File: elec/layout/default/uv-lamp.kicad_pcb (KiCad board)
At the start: 2 copper layers, 21 x 21 mm, 3 parts, among them U1 ?, U2 ?, U3 ?

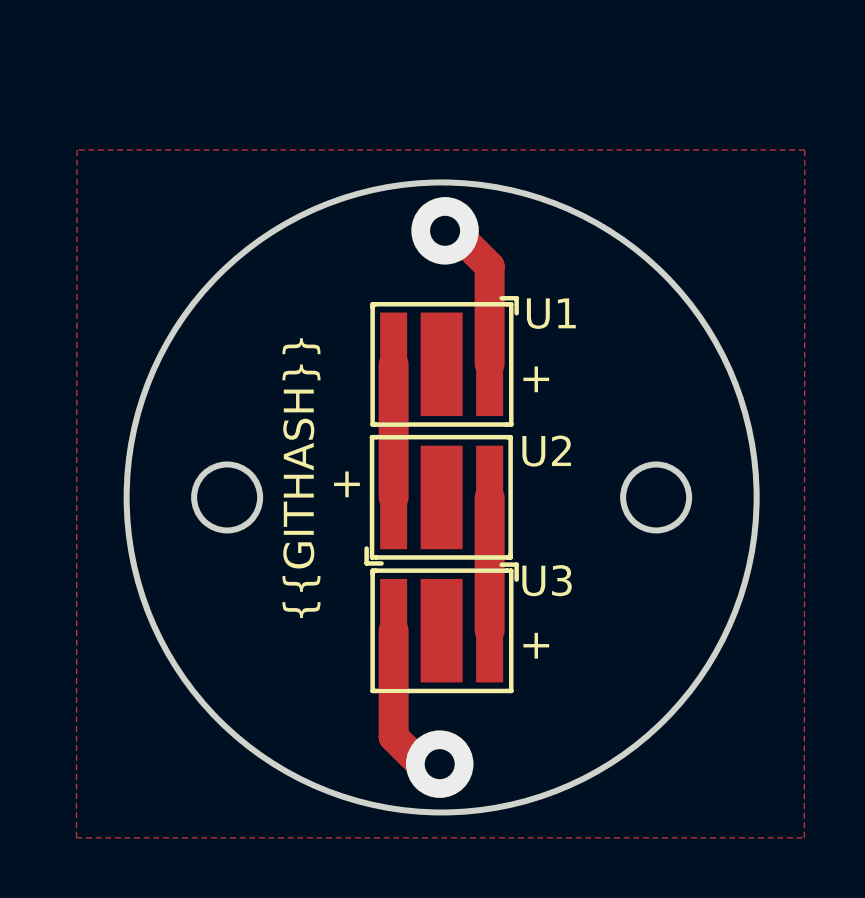
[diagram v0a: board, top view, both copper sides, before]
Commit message: adding notches to driver
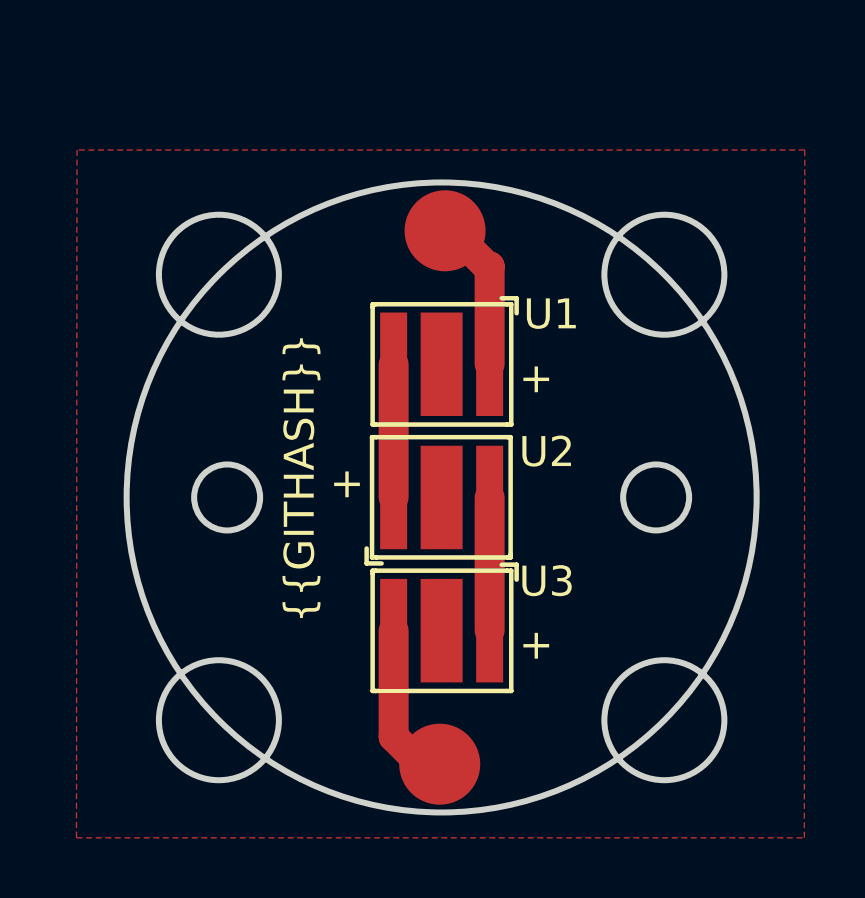
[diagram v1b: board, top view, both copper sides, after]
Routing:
- net gnd: track 5.58 -> 5.45 mm, vias 1 -> 0
- net vcc: track 5.36 -> 5.40 mm, vias 1 -> 0
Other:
- outline, holes or cut-outs redrawn
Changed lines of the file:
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@@
+	)
+	(gr_circle
+		(center 148.004527 77.420557)
+		(end 149.254527 77.420557)
+		(stroke
+			(width 0.2)
+			(type solid)
+		)
+		(fill solid)
+		(layer "F.Cu")
+		(net 4)
+	)
+	(gr_circle
+		(center 147.826005 95.201)
+		(end 149.076005 95.201)
+		(stroke
+			(width 0.2)
+			(type solid)
+		)
+		(fill solid)
+		(layer "F.Cu")
+		(net 7)
+	)
+	(gr_circle
+		(center 155.314621 78.885379)
+		(end 157.314621 78.885379)
+		(stroke
+			(width 0.2)
+			(type default)
+		)
+		(fill none)
+		(layer "Edge.Cuts")
 	)
 	(gr_circle
@@
 	)
 	(gr_circle
+		(center 140.465379 93.734621)
+		(end 142.465379 93.734621)
+		(stroke
+			(width 0.2)
+			(type default)
+		)
+		(fill none)
+		(layer "Edge.Cuts")
+	)
+	(gr_circle
 		(center 140.74 86.31)
 		(end 141.84 86.31)
+		(stroke
+			(width 0.2)
+			(type default)
+		)
+		(fill none)
+		(layer "Edge.Cuts")
+	)
+	(gr_circle
+		(center 155.314621 93.734621)
+		(end 157.314621 93.734621)
+		(stroke
+			(width 0.2)
+			(type default)
+		)
+		(fill none)
+		(layer "Edge.Cuts")
+	)
+	(gr_circle
+		(center 140.465379 78.885379)
+		(end 142.465379 78.885379)
 		(stroke
 			(width 0.2)
@@
 	)
 	(segment
-		(start 149.49 78.60703)
-		(end 148.004527 77.121557)
+		(start 148.075 77.275)
+		(end 149.40703 78.60703)
+		(width 1)
+		(layer "F.Cu")
+		(net 4)
+	)
+	(segment
+		(start 148.004527 77.420557)
+		(end 148.004527 77.345473)
 		(width 1)
 		(layer "F.Cu")
@@
 		(net 4)
 	)
-	(via
-		(at 148.004527 77.421557)
-		(size 2.25)
-		(drill 1)
-		(layers "F.Cu" "B.Cu")
-		(free yes)
-		(teardrops
-			(best_length_ratio 0.5)
-			(max_length 1)
-			(best_width_ratio 1)
-			(max_width 2)
-			(curve_points 0)
-			(filter_ratio 0.9)
-			(enabled yes)
-			(allow_two_segments yes)
-			(prefer_zone_connections yes)
-		)
+	(segment
+		(start 149.40703 78.60703)
+		(end 149.49 78.60703)
+		(width 1)
+		(layer "F.Cu")
+		(net 4)
+	)
+	(segment
+		(start 148.004527 77.345473)
+		(end 148.075 77.275)
+		(width 1)
+		(layer "F.Cu")
 		(net 4)
 	)
@@
 	)
 	(segment
+		(start 147.826005 95.201)
+		(end 147.201 95.201)
+		(width 1)
+		(layer "F.Cu")
+		(net 7)
+	)
+	(segment
 		(start 146.29 94.29)
 		(end 146.29 90.75)
@@
 	)
 	(segment
-		(start 147.826005 95.5)
-		(end 147.5 95.5)
-		(width 1)
-		(layer "F.Cu")
-		(net 7)
-	)
-	(segment
-		(start 147.5 95.5)
+		(start 147.201 95.201)
 		(end 146.29 94.29)
 		(width 1)
 		(layer "F.Cu")
-		(net 7)
-	)
-	(via
-		(at 147.826005 95.2)
-		(size 2.25)
-		(drill 1)
-		(layers "F.Cu" "B.Cu")
-		(free yes)
-		(teardrops
-			(best_length_ratio 0.5)
-			(max_length 1)
-			(best_width_ratio 1)
-			(max_width 2)
-			(curve_points 0)
-			(filter_ratio 0.9)
-			(enabled yes)
-			(allow_two_segments yes)
-			(prefer_zone_connections yes)
-		)
 		(net 7)
 	)
@@
 			)
 		)
-	)
-	(zone
-		(net 0)
-		(net_name "")
-		(layer "F.Cu")
-		(name "$teardrop_padvia$")
-		(hatch full 0.1)
-		(priority 30000)
-		(attr
-			(teardrop
-				(type padvia)
-			)
-		)
-		(connect_pads yes
-			(clearance 0)
-		)
-		(min_thickness 0.0254)
-		(filled_areas_thickness no)
-		(fill yes
-			(thermal_gap 0.5)
-			(thermal_bridge_width 0.5)
-			(island_removal_mode 1)
-			(island_area_min 10)
-		)
-		(polygon
-			(pts
-				(xy 148.99 78.808537) (xy 149.99 78.808537) (xy 149.062304 77.040318) (xy 148.004527 77.420557)
-				(xy 147.809173 78.529466)
-			)
-		)
-	)
-	(zone
-		(net 0)
-		(net_name "")
-		(layer "F.Cu")
-		(name "$teardrop_padvia$")
-		(hatch full 0.1)
-		(priority 30001)
-		(attr
-			(teardrop
-				(type padvia)
-			)
-		)
-		(connect_pads yes
-			(clearance 0)
-		)
-		(min_thickness 0.0254)
-		(filled_areas_thickness no)
-		(fill yes
-			(thermal_gap 0.5)
-			(thermal_bridge_width 0.5)
-			(island_removal_mode 1)
-			(island_area_min 10)
-		)
-		(polygon
-			(pts
-				(xy 146.79 93.991203) (xy 145.79 93.991203) (xy 146.828693 95.688423) (xy 147.826005 95.201) (xy 148.021359 94.092091)
-			)
-		)
-	)
-	(zone
-		(net 4)
-		(net_name "vcc")
-		(layer "F.Cu")
-		(name "$teardrop_padvia$")
-		(hatch full 0.1)
-		(priority 30000)
-		(attr
-			(teardrop
-				(type padvia)
-			)
-		)
-		(connect_pads yes
-			(clearance 0)
-		)
-		(min_thickness 0.0254)
-		(filled_areas_thickness no)
-		(fill yes
-			(thermal_gap 0.5)
-			(thermal_bridge_width 0.5)
-			(island_removal_mode 1)
-			(island_area_min 10)
-		)
-		(polygon
-			(pts
-				(xy 148.99 78.808537) (xy 149.99 78.808537) (xy 149.062304 77.040318) (xy 148.004527 77.420557)
-				(xy 147.809173 78.529466)
-			)
-		)
-	)
-	(zone
-		(net 4)
-		(net_name "vcc")
-		(layer "F.Cu")
-		(name "$teardrop_padvia$")
-		(hatch full 0.1)
-		(priority 30000)
-		(attr
-			(teardrop
-				(type padvia)
-			)
-		)
-		(connect_pads yes
-			(clearance 0)
-		)
-		(min_thickness 0.0254)
-		(filled_areas_thickness no)
-		(fill yes
-			(thermal_gap 0.5)
-			(thermal_bridge_width 0.5)
-			(island_removal_mode 1)
-			(island_area_min 10)
-		)
-		(polygon
-			(pts
-				(xy 148.99 78.808537) (xy 149.99 78.808537) (xy 149.062304 77.040318) (xy 148.004527 77.420557)
-				(xy 147.809173 78.529466)
-			)
-		)

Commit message: new uv PCB
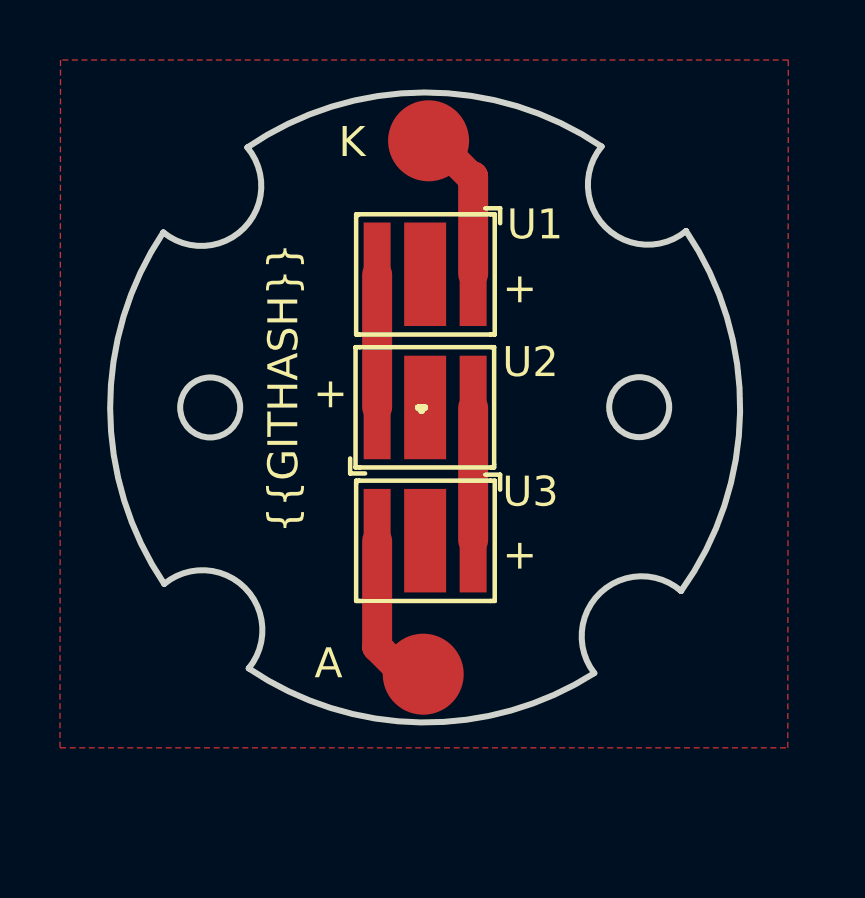
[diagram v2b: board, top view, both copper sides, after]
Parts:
- moved U1 3.05 mm to (147.3, 78.9)
- moved U2 3.05 mm to (147.3, 83.3)
- moved U3 3.05 mm to (147.3, 87.8)
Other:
- outline, holes or cut-outs redrawn
- board text added: "A"
- board text added: "K"
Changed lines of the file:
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@@
 	(footprint "lib:LED-SMD_3P-L3.5-W3.5_M3535O1IRS13G06"
 		(layer "F.Cu")
-		(at 147.89 90.75)
+		(at 147.34 87.75)
 		(property "Reference" "U3"
 			(at 3.51 -1.63 0)
@@
 	(footprint "lib:LED-SMD_3P-L3.5-W3.5_M3535O1IRS13G06"
 		(layer "F.Cu")
-		(at 147.89 81.87)
+		(at 147.34 78.87)
 		(property "Reference" "U1"
 			(at 3.66 -1.66 0)
@@
 	(footprint "lib:LED-SMD_3P-L3.5-W3.5_M3535O1IRS13G06"
 		(layer "F.Cu")
-		(at 147.89 86.31 180)
+		(at 147.34 83.31 180)
 		(property "Reference" "U2"
 			(at -3.51 1.51 0)
@@
 	)
 	(gr_circle
-		(center 148.004527 77.420557)
-		(end 149.254527 77.420557)
+		(center 147.454527 74.420557)
+		(end 148.704527 74.420557)
 		(stroke
 			(width 0.2)
@@
 	)
 	(gr_circle
-		(center 147.826005 95.201)
-		(end 149.076005 95.201)
+		(center 147.276005 92.201)
+		(end 148.526005 92.201)
 		(stroke
 			(width 0.2)
@@
 		(net 7)
 	)
+	(gr_line
+		(start 147.339996 83.310002)
+		(end 147.218594 83.431404)
+		(stroke
+			(width 0.2)
+			(type default)
+		)
+		(layer "F.SilkS")
+	)
+	(gr_line
+		(start 147.339996 83.310002)
+		(end 147.099872 83.310002)
+		(stroke
+			(width 0.2)
+			(type default)
+		)
+		(layer "F.SilkS")
+	)
+	(gr_line
+		(start 147.339996 83.310002)
+		(end 147.099872 83.310002)
+		(stroke
+			(width 0.2)
+			(type default)
+		)
+		(layer "F.SilkS")
+	)
+	(gr_line
+		(start 147.218594 83.431404)
+		(end 147.099872 83.310002)
+		(stroke
+			(width 0.2)
+			(type default)
+		)
+		(layer "F.SilkS")
+	)
 	(gr_circle
-		(center 155.314621 78.885379)
-		(end 157.314621 78.885379)
+		(center 147.454527 74.420557)
+		(end 148.704527 74.420557)
+		(stroke
+			(width 0.2)
+			(type solid)
+		)
+		(fill solid)
+		(layer "F.Mask")
+	)
+	(gr_circle
+		(center 147.276005 92.201)
+		(end 148.526005 92.201)
+		(stroke
+			(width 0.2)
+			(type solid)
+		)
+		(fill solid)
+		(layer "F.Mask")
+	)
+	(gr_arc
+		(start 141.413031 74.64276)
+		(mid 147.312897 72.810037)
+		(end 153.222145 74.612282)
+		(stroke
+			(width 0.2)
+			(type default)
+		)
+		(layer "Edge.Cuts")
+	)
+	(gr_arc
+		(start 152.980661 92.166237)
+		(mid 153.182794 89.483469)
+		(end 155.872617 89.429183)
+		(stroke
+			(width 0.2)
+			(type default)
+		)
+		(layer "Edge.Cuts")
+	)
+	(gr_arc
+		(start 156.037716 77.427853)
+		(mid 157.839003 83.454433)
+		(end 155.872617 89.429183)
+		(stroke
+			(width 0.2)
+			(type default)
+		)
+		(layer "Edge.Cuts")
+	)
+	(gr_circle
+		(center 140.175 83.310002)
+		(end 141.175 83.310002)
 		(stroke
 			(width 0.2)
@@
 		(layer "Edge.Cuts")
 	)
+	(gr_arc
+		(start 152.980661 92.166237)
+		(mid 147.195564 93.809009)
+		(end 141.457847 92.007721)
+		(stroke
+			(width 0.2)
+			(type default)
+		)
+		(layer "Edge.Cuts")
+	)
+	(gr_arc
+		(start 141.413031 74.64276)
+		(mid 141.30115 77.333592)
+		(end 138.611627 77.47343)
+		(stroke
+			(width 0.2)
+			(type default)
+		)
+		(layer "Edge.Cuts")
+	)
+	(gr_arc
+		(start 138.642277 89.192151)
+		(mid 136.840032 83.337464)
+		(end 138.611627 77.47343)
+		(stroke
+			(width 0.2)
+			(type default)
+		)
+		(layer "Edge.Cuts")
+	)
+	(gr_arc
+		(start 156.037716 77.427853)
+		(mid 153.350405 77.299593)
+		(end 153.222145 74.612282)
+		(stroke
+			(width 0.2)
+			(type default)
+		)
+		(layer "Edge.Cuts")
+	)
 	(gr_circle
-		(center 155.04 86.31)
-		(end 156.14 86.31)
+		(center 154.475 83.3)
+		(end 155.475 83.3)
 		(stroke
 			(width 0.2)
@@
 		(layer "Edge.Cuts")
 	)
-	(gr_circle
-		(center 147.89 86.31)
-		(end 158.39 86.31)
-		(stroke
-			(width 0.2)
-			(type default)
-		)
-		(fill none)
+	(gr_arc
+		(start 138.642277 89.192151)
+		(mid 141.329577 89.32042)
+		(end 141.457847 92.007721)
+		(stroke
+			(width 0.2)
+			(type default)
+		)
 		(layer "Edge.Cuts")
 	)
-	(gr_circle
-		(center 140.465379 93.734621)
-		(end 142.465379 93.734621)
-		(stroke
-			(width 0.2)
-			(type default)
-		)
-		(fill none)
-		(layer "Edge.Cuts")
-	)
-	(gr_circle
-		(center 140.74 86.31)
-		(end 141.84 86.31)
-		(stroke
-			(width 0.2)
-			(type default)
-		)
-		(fill none)
-		(layer "Edge.Cuts")
-	)
-	(gr_circle
-		(center 155.314621 93.734621)
-		(end 157.314621 93.734621)
-		(stroke
-			(width 0.2)
-			(type default)
-		)
-		(fill none)
-		(layer "Edge.Cuts")
-	)
-	(gr_circle
-		(center 140.465379 78.885379)
-		(end 142.465379 78.885379)
-		(stroke
-			(width 0.2)
-			(type default)
-		)
-		(fill none)
-		(layer "Edge.Cuts")
+	(gr_text "K"
+		(at 144.454527 75.05 0)
+		(layer "F.SilkS")
+		(effects
+			(font
+				(size 1 1)
+				(thickness 0.15)
+			)
+			(justify left bottom)
+		)
+	)
+	(gr_text "A"
+		(at 143.65 92.425 0)
+		(layer "F.SilkS")
+		(effects
+			(font
+				(size 1 1)
+				(thickness 0.15)
+			)
+			(justify left bottom)
+		)
 	)
 	(gr_text "{{GITHASH}}"
-		(at 143.75 90.5 90)
+		(at 143.2 87.5 90)
 		(layer "F.SilkS")
 		(effects
@@
 	)
 	(segment
-		(start 148.075 77.275)
-		(end 149.40703 78.60703)
+		(start 147.525 74.275)
+		(end 148.85703 75.60703)
 		(width 1)
 		(layer "F.Cu")
@@
 	)
 	(segment
-		(start 148.004527 77.420557)
-		(end 148.004527 77.345473)
+		(start 147.454527 74.420557)
+		(end 147.454527 74.345473)
 		(width 1)
 		(layer "F.Cu")
@@
 	)
 	(segment
-		(start 149.49 81.87)
-		(end 149.49 78.60703)
+		(start 148.94 78.87)
+		(end 148.94 75.60703)
 		(width 1)
 		(layer "F.Cu")
@@
 	)
 	(segment
-		(start 149.40703 78.60703)
-		(end 149.49 78.60703)
+		(start 148.85703 75.60703)
+		(end 148.94 75.60703)
 		(width 1)
 		(layer "F.Cu")
@@
 	)
 	(segment
-		(start 148.004527 77.345473)
-		(end 148.075 77.275)
+		(start 147.454527 74.345473)
+		(end 147.525 74.275)
 		(width 1)
 		(layer "F.Cu")
@@
 	)
 	(segment
-		(start 146.29 81.87)
-		(end 146.29 86.31)
+		(start 145.74 78.87)
+		(end 145.74 83.31)
 		(width 1)
 		(layer "F.Cu")
@@
 	)
 	(segment
-		(start 149.49 90.75)
-		(end 149.49 86.31)
+		(start 148.94 87.75)
+		(end 148.94 83.31)
 		(width 1)
 		(layer "F.Cu")
@@
 	)
 	(segment
-		(start 147.826005 95.201)
-		(end 147.201 95.201)
+		(start 147.276005 92.201)
+		(end 146.651 92.201)
 		(width 1)
 		(layer "F.Cu")
@@
 	)
 	(segment
-		(start 146.29 94.29)
-		(end 146.29 90.75)
+		(start 145.74 91.29)
+		(end 145.74 87.75)
 		(width 1)
 		(layer "F.Cu")
@@
 	)
 	(segment
-		(start 147.201 95.201)
-		(end 146.29 94.29)
+		(start 146.651 92.201)
+		(end 145.74 91.29)
 		(width 1)
 		(layer "F.Cu")
@@
 		(polygon
 			(pts
-				(xy 159.995473 74.727755) (xy 135.735473 74.727755) (xy 135.718641 97.655363) (xy 159.978641 97.655363)
-			)
-		)
-	)
+				(xy 159.445473 71.727755) (xy 135.185473 71.727755) (xy 135.168641 94.655363) (xy 159.428641 94.655363)
+			)
+		)
+	)
+	(group "EDGE"
+		(members "3f32955a-13c8-4494-8d4c-f41d730cb676" "4272d73d-cbca-430f-8818-96db903f9f1f"
+			"437f0d91-3824-4e78-ac65-7362dd4f45e3" "4ee99006-ee5a-4b5a-b8b7-b9ab914d1592"
+			"5cff338f-943d-4e98-88b1-9f6947ca795d" "7c7b39ac-6e04-4c63-b45f-57d735149198"
+			"8f8cb0ab-8f0a-4976-993b-5847a34d43a5" "9c499254-1d89-42db-a243-b0f8ac74d3c7"
+			"a26efc3e-8797-498b-89f7-85eca495796e" "b53f9cd2-7b3c-4b08-8673-0979f11b6317"
+			"bfc79c8f-9dc6-4218-80d1-0bf2bfc0d38e" "d504e386-bd7a-4752-afef-8b62739e810b"
+			"d6f6a9a7-dda4-4acc-ab45-cc71e4650824" "ea87b53b-528e-48f9-86c0-03e332587b25"
+		)
+	)

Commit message: ccdriver
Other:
- outline, holes or cut-outs redrawn
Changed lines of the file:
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@@
 	(gr_circle
 		(center 140.175 83.310002)
-		(end 141.175 83.310002)
+		(end 141.225 83.310002)
 		(stroke
 			(width 0.2)
@@
 	(gr_circle
 		(center 154.475 83.3)
-		(end 155.475 83.3)
+		(end 155.525 83.3)
 		(stroke
 			(width 0.2)

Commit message: error checking
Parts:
- U1, U2, U3: value ? -> (none)
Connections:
- net led1-k renamed A-1
- net led2-k renamed K
- net vcc renamed A
- U1 pad 3: led1-_3 -> (no net)
- U2 pad 3: led2-_3 -> (no net)
- U3 pad 3: led3-_3 -> (no net)
